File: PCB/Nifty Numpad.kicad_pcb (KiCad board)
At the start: 4 copper layers, 118.4 x 129.7 mm, 176 parts, among them J101 SWD, J102 USB-C, J103 UART, SW101 PTS636 SL43 SMTR LFS, SW102 PTS636 SL43 SMTR LFS, SW301 M1, SW302 M7, SW303 F13, SW304 F14, SW305 F15, SW306 F16, SW307 M2, SW308 M8, SW309 Num Toggle, SW310 /, SW311 *, SW312 -, SW313 M3, SW314 M9, SW315 7, SW316 8, SW317 9, SW318 +, SW319 M4, SW320 M10, SW321 4, SW322 5, SW323 6, SW324 M5, SW325 M11, SW326 1, SW327 2, SW328 3, SW329 Enter, SW330 M6, SW331 M12, SW332 0, SW333 ., U101 MIC5366-3.3YC5, U102 CM1213A−02Sx, U103 SN74LVC1T45DCK, U104 RP2040, U105 W25Q40CLSNIG, Y101 ABLS-12.000MHZ-B4-T

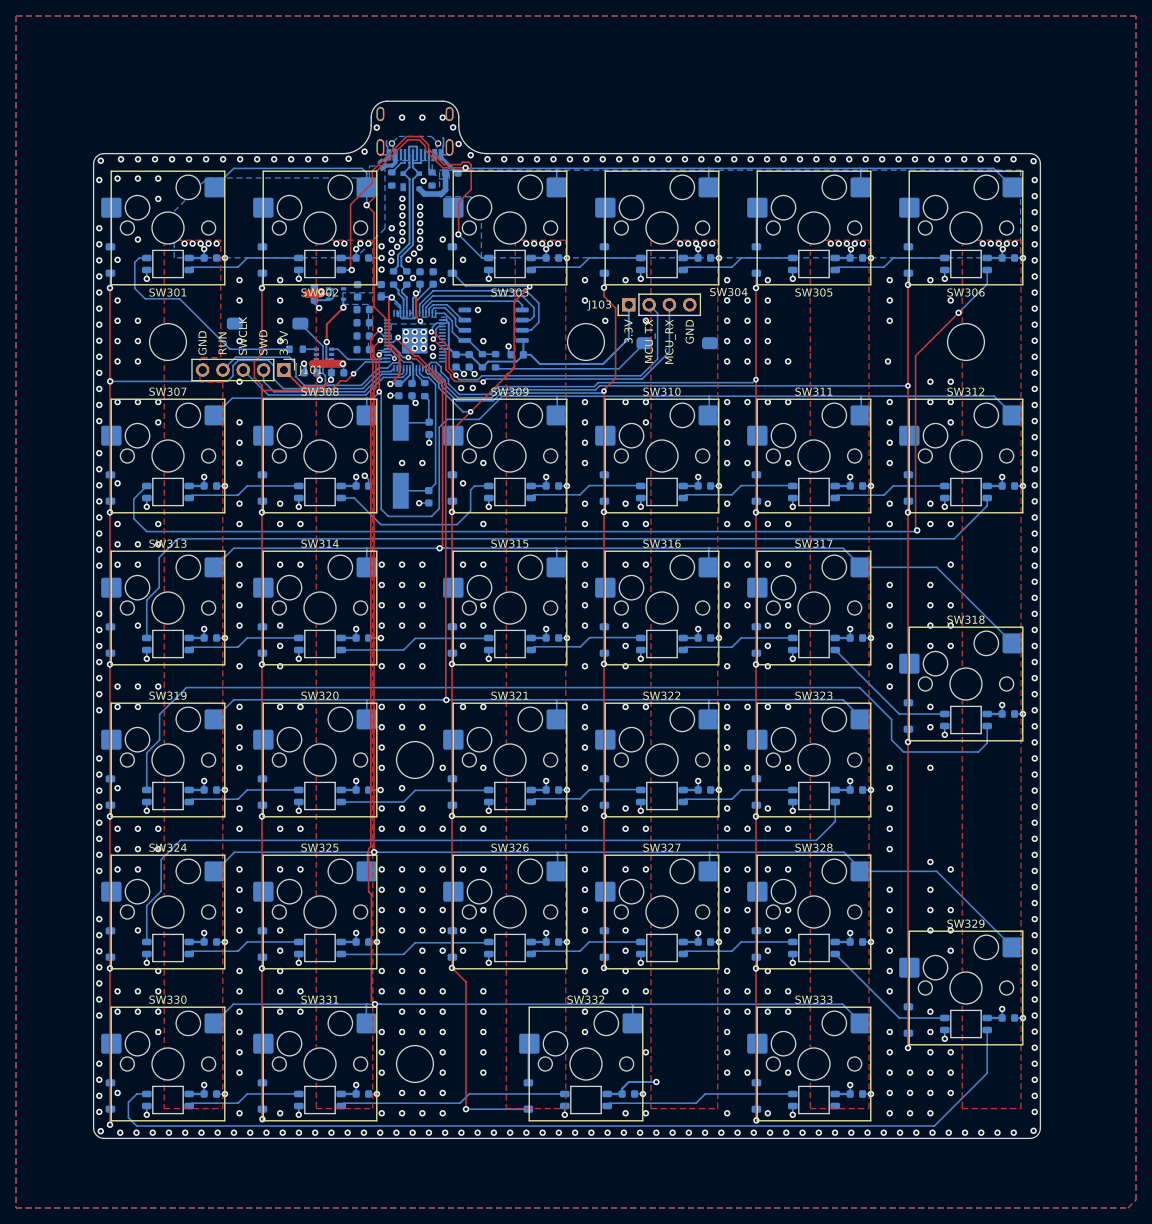
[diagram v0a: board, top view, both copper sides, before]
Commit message: Fixed LED rotation, beefed up standoffs, added docs
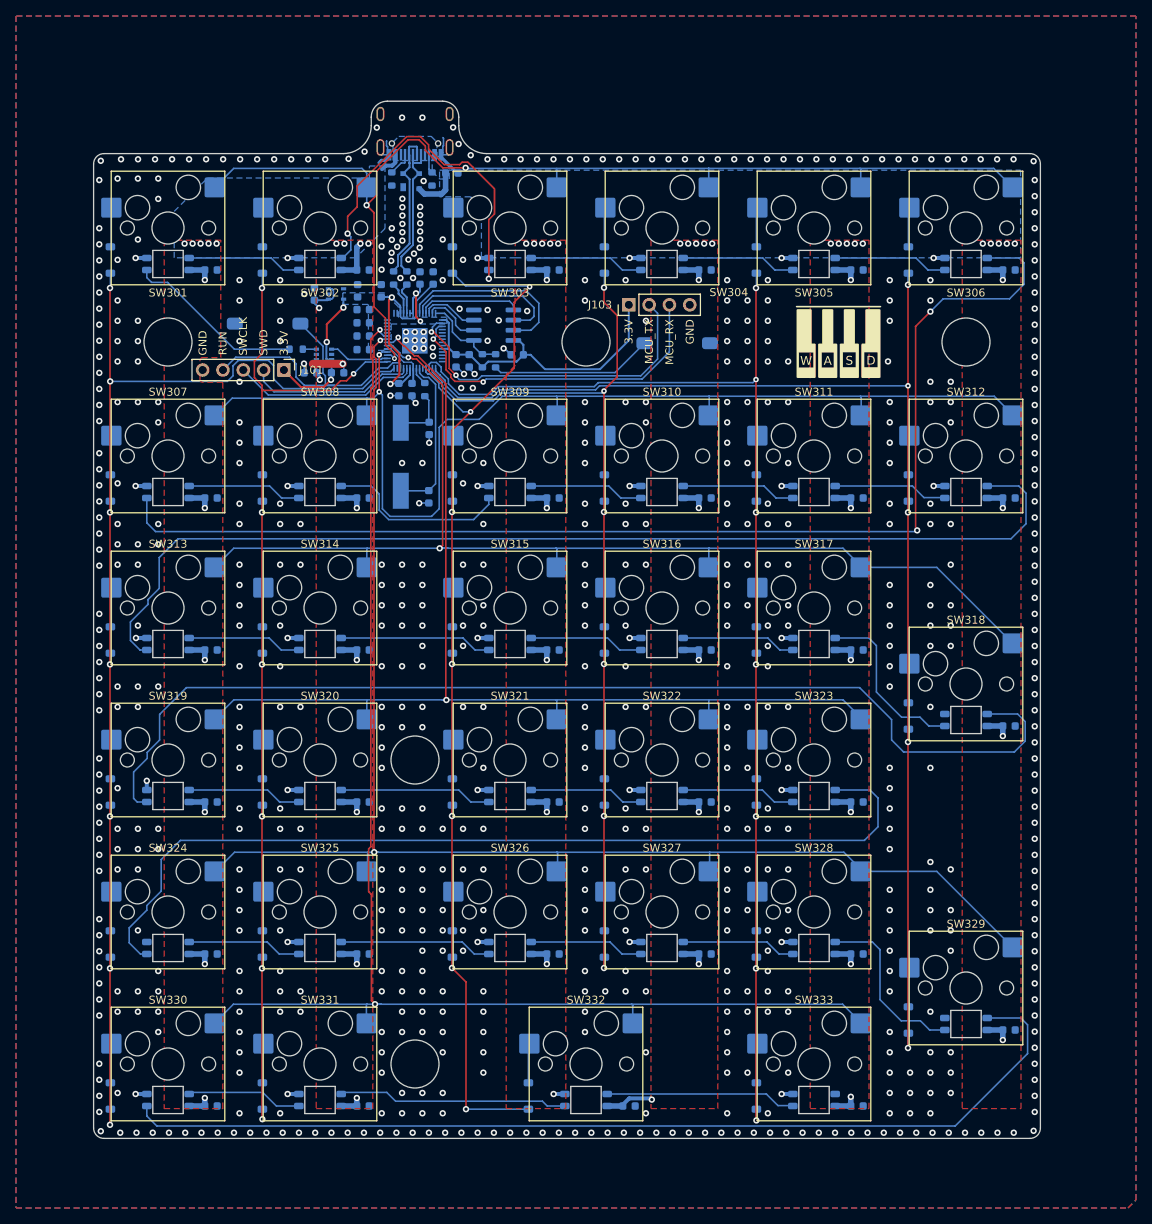
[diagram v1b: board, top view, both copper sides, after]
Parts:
- D201, D202, D203, D204, D205, D206, D207, D208, D209, D210, D211, D212, D213, D214, D215, D216, D217, D218, D219, D220, D221, D222, D223, D224, D225, D226, D227, D228, D229, D230, D231, D232, D233: value SK6812-E -> SK6805MINI-E
- H101, H102, H103, H104, H105: value 4.60mm -> 6.00mm; footprint irex_MountingHole:MountingHole_4.6mm_ReducedCourtyard -> irex_MountingHole:MountingHole_6.0mm_ReducedCourtyard
- U105: footprint Package_SO:SOIC-8_5.275x5.275mm_P1.27mm -> Package_SO:SOIC-8_3.9x4.9mm_P1.27mm
- moved C201 1.50 mm to (167.4, 88.8)
- moved C202 1.50 mm to (186.4, 88.8)
- moved C203 1.50 mm to (210.1, 88.8)
- moved C204 1.50 mm to (229.1, 88.8)
- moved C205 1.50 mm to (248.1, 88.8)
- moved C206 1.50 mm to (267.1, 88.8)
- moved C207 1.50 mm to (167.4, 117.2)
- moved C208 1.50 mm to (186.4, 117.2)
- moved C209 1.50 mm to (210.1, 117.2)
- moved C210 1.50 mm to (229.1, 117.2)
- moved C211 1.50 mm to (248.1, 117.2)
- moved C212 1.50 mm to (267.1, 117.2)
- moved C213 1.50 mm to (167.4, 136.2)
- moved C214 1.50 mm to (186.4, 136.2)
- moved C215 1.50 mm to (210.1, 136.2)
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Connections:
- D201 pad 1: GND -> +5V
- D201 pad 2: /LED Matrix/DIN0 -> Net-(D201-DOUT)
- D201 pad 3: +5V -> GND
- D201 pad 4: Net-(D201-DOUT) -> /LED Matrix/DIN0
- D202 pad 1: GND -> +5V
- D202 pad 2: Net-(D201-DOUT) -> Net-(D202-DOUT)
- D202 pad 3: +5V -> GND
- D202 pad 4: Net-(D202-DOUT) -> Net-(D201-DOUT)
- D203 pad 1: GND -> +5V
- D203 pad 2: Net-(D202-DOUT) -> Net-(D203-DOUT)
- D203 pad 3: +5V -> GND
- D203 pad 4: Net-(D203-DOUT) -> Net-(D202-DOUT)
- D204 pad 1: GND -> +5V
- D204 pad 2: Net-(D203-DOUT) -> Net-(D204-DOUT)
- D204 pad 3: +5V -> GND
- D204 pad 4: Net-(D204-DOUT) -> Net-(D203-DOUT)
- D205 pad 1: GND -> +5V
- D205 pad 2: Net-(D204-DOUT) -> Net-(D205-DOUT)
- D205 pad 3: +5V -> GND
- D205 pad 4: Net-(D205-DOUT) -> Net-(D204-DOUT)
- D206 pad 1: GND -> +5V
- D206 pad 2: Net-(D205-DOUT) -> Net-(D206-DOUT)
- D206 pad 3: +5V -> GND
- D206 pad 4: Net-(D206-DOUT) -> Net-(D205-DOUT)
- D207 pad 1: GND -> +5V
- D207 pad 2: Net-(D206-DOUT) -> Net-(D207-DOUT)
- D207 pad 3: +5V -> GND
- D207 pad 4: Net-(D207-DOUT) -> Net-(D206-DOUT)
- D208 pad 1: GND -> +5V
- D208 pad 2: Net-(D207-DOUT) -> Net-(D208-DOUT)
- D208 pad 3: +5V -> GND
- D208 pad 4: Net-(D208-DOUT) -> Net-(D207-DOUT)
- D209 pad 1: GND -> +5V
- D209 pad 2: Net-(D208-DOUT) -> Net-(D209-DOUT)
- D209 pad 3: +5V -> GND
- D209 pad 4: Net-(D209-DOUT) -> Net-(D208-DOUT)
- D210 pad 1: GND -> +5V
- D210 pad 2: Net-(D209-DOUT) -> Net-(D210-DOUT)
- D210 pad 3: +5V -> GND
- D210 pad 4: Net-(D210-DOUT) -> Net-(D209-DOUT)
- D211 pad 1: GND -> +5V
- D211 pad 2: Net-(D210-DOUT) -> Net-(D211-DOUT)
- D211 pad 3: +5V -> GND
- D211 pad 4: Net-(D211-DOUT) -> Net-(D210-DOUT)
- D212 pad 1: GND -> +5V
- D212 pad 2: Net-(D211-DOUT) -> Net-(D212-DOUT)
- D212 pad 3: +5V -> GND
- D212 pad 4: Net-(D212-DOUT) -> Net-(D211-DOUT)
- D213 pad 1: GND -> +5V
- D213 pad 2: Net-(D212-DOUT) -> Net-(D213-DOUT)
- D213 pad 3: +5V -> GND
- D213 pad 4: Net-(D213-DOUT) -> Net-(D212-DOUT)
- D214 pad 1: GND -> +5V
- D214 pad 2: Net-(D213-DOUT) -> Net-(D214-DOUT)
- D214 pad 3: +5V -> GND
- D214 pad 4: Net-(D214-DOUT) -> Net-(D213-DOUT)
- D215 pad 1: GND -> +5V
- D215 pad 2: Net-(D214-DOUT) -> Net-(D215-DOUT)
- D215 pad 3: +5V -> GND
- D215 pad 4: Net-(D215-DOUT) -> Net-(D214-DOUT)
- D216 pad 1: GND -> +5V
- D216 pad 2: Net-(D215-DOUT) -> Net-(D216-DOUT)
- D216 pad 3: +5V -> GND
- D216 pad 4: Net-(D216-DOUT) -> Net-(D215-DOUT)
- D217 pad 1: GND -> +5V
- D217 pad 2: Net-(D216-DOUT) -> Net-(D217-DOUT)
- D217 pad 3: +5V -> GND
- D217 pad 4: Net-(D217-DOUT) -> Net-(D216-DOUT)
- D218 pad 1: GND -> +5V
- D218 pad 2: Net-(D217-DOUT) -> Net-(D218-DOUT)
- D218 pad 3: +5V -> GND
- D218 pad 4: Net-(D218-DOUT) -> Net-(D217-DOUT)
- D219 pad 1: GND -> +5V
- D219 pad 2: Net-(D218-DOUT) -> Net-(D219-DOUT)
- D219 pad 3: +5V -> GND
- D219 pad 4: Net-(D219-DOUT) -> Net-(D218-DOUT)
- D220 pad 1: GND -> +5V
- D220 pad 2: Net-(D219-DOUT) -> Net-(D220-DOUT)
- D220 pad 3: +5V -> GND
- D220 pad 4: Net-(D220-DOUT) -> Net-(D219-DOUT)
- D221 pad 1: GND -> +5V
- D221 pad 2: Net-(D220-DOUT) -> Net-(D221-DOUT)
- D221 pad 3: +5V -> GND
- D221 pad 4: Net-(D221-DOUT) -> Net-(D220-DOUT)
- D222 pad 1: GND -> +5V
- D222 pad 2: Net-(D221-DOUT) -> Net-(D222-DOUT)
- D222 pad 3: +5V -> GND
- D222 pad 4: Net-(D222-DOUT) -> Net-(D221-DOUT)
- D223 pad 1: GND -> +5V
- D223 pad 2: Net-(D222-DOUT) -> Net-(D223-DOUT)
- D223 pad 3: +5V -> GND
- D223 pad 4: Net-(D223-DOUT) -> Net-(D222-DOUT)
- D224 pad 1: GND -> +5V
- D224 pad 2: Net-(D223-DOUT) -> Net-(D224-DOUT)
- D224 pad 3: +5V -> GND
- D224 pad 4: Net-(D224-DOUT) -> Net-(D223-DOUT)
- D225 pad 1: GND -> +5V
- D225 pad 2: Net-(D224-DOUT) -> Net-(D225-DOUT)
- D225 pad 3: +5V -> GND
- D225 pad 4: Net-(D225-DOUT) -> Net-(D224-DOUT)
- D226 pad 1: GND -> +5V
- D226 pad 2: Net-(D225-DOUT) -> Net-(D226-DOUT)
- D226 pad 3: +5V -> GND
- D226 pad 4: Net-(D226-DOUT) -> Net-(D225-DOUT)
- D227 pad 1: GND -> +5V
- D227 pad 2: Net-(D226-DOUT) -> Net-(D227-DOUT)
- D227 pad 3: +5V -> GND
- D227 pad 4: Net-(D227-DOUT) -> Net-(D226-DOUT)
- D228 pad 1: GND -> +5V
- D228 pad 2: Net-(D227-DOUT) -> Net-(D228-DOUT)
- D228 pad 3: +5V -> GND
- D228 pad 4: Net-(D228-DOUT) -> Net-(D227-DOUT)
- D229 pad 1: GND -> +5V
- D229 pad 2: Net-(D228-DOUT) -> Net-(D229-DOUT)
- D229 pad 3: +5V -> GND
- D229 pad 4: unconnected-(D229-DOUT-Pad4) -> Net-(D228-DOUT)
- D230 pad 1: GND -> +5V
- D230 pad 2: unconnected-(D229-DOUT-Pad4) -> Net-(D230-DOUT)
- D230 pad 3: +5V -> GND
- D230 pad 4: Net-(D230-DOUT) -> Net-(D229-DOUT)
- D231 pad 1: GND -> +5V
- D231 pad 2: Net-(D230-DOUT) -> Net-(D231-DOUT)
- D231 pad 3: +5V -> GND
- D231 pad 4: Net-(D231-DOUT) -> Net-(D230-DOUT)
- D232 pad 1: GND -> +5V
- D232 pad 2: Net-(D231-DOUT) -> Net-(D232-DOUT)
- D232 pad 3: +5V -> GND
- D232 pad 4: Net-(D232-DOUT) -> Net-(D231-DOUT)
- D233 pad 1: GND -> +5V
- D233 pad 2: Net-(D232-DOUT) -> unconnected-(D233-DOUT-Pad2)
- D233 pad 3: +5V -> GND
- D233 pad 4: unconnected-(D233-DOUT-Pad4) -> Net-(D232-DOUT)
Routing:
- net Net-(D229-DOUT): track 0.00 -> 124.6 mm
- net unconnected-(D229-DOUT-Pad4): track 120.6 -> 0.00 mm
- net GND: track 101.5 -> 67.5 mm, vias 770 -> 724
- net Net-(D223-DOUT): track 99.7 -> 115.5 mm
- net Net-(D212-DOUT): track 117.9 -> 133.5 mm
- net Net-(D218-DOUT): track 122.4 -> 136.3 mm
- net Net-(D206-DOUT): track 139.8 -> 148.8 mm
- net +5V: track 120.1 -> 127.1 mm, vias 64 -> 63
- net /LED Matrix/DIN0: track 27.5 -> 22.5 mm
- net Net-(D228-DOUT): track 17.0 -> 21.9 mm
- net Net-(D217-DOUT): track 17.0 -> 21.7 mm
- net +3.3V: track 70.7 -> 72.3 mm
- net /QSPI_CLK: track 18.7 -> 19.8 mm
- net /QSPI_SD3: track 22.2 -> 23.3 mm
- net /QSPI_SD2: track 6.03 -> 7.16 mm
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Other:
- board text added: "${REV}"
- board text added: "A"
- board text added: "D"
- board text added: "Designed by I. Rex Rev ${REV} Jun 2023"
- board text added: "S"
- board text added: "W"
- board text removed: "Designed by I. Rex Rev 0 Jun 2023"
